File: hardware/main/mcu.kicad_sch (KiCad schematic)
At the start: 15 parts, among them Q9 SSM3J338R, U1 Holyiot-18010-NRF52840

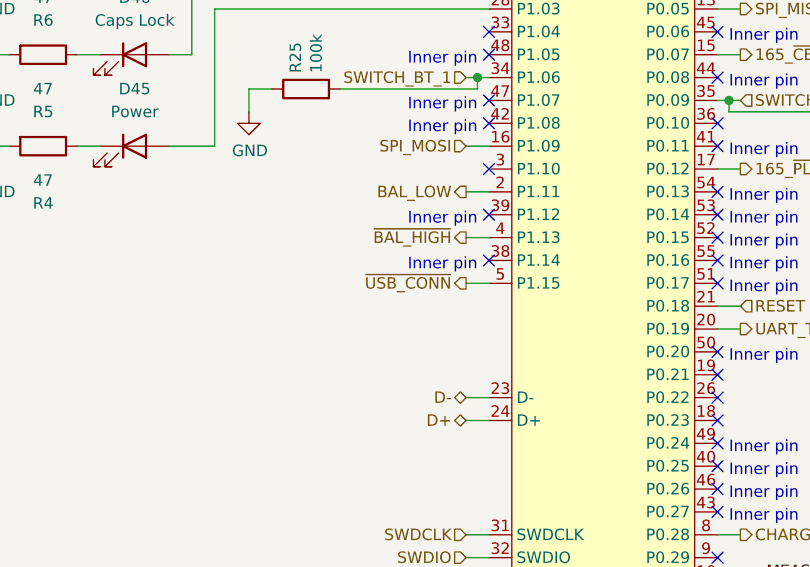
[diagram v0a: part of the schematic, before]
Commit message: Remove the USB sense curcuit
As V_BUS is connected to the MCU it can detect when the USB is
connected.
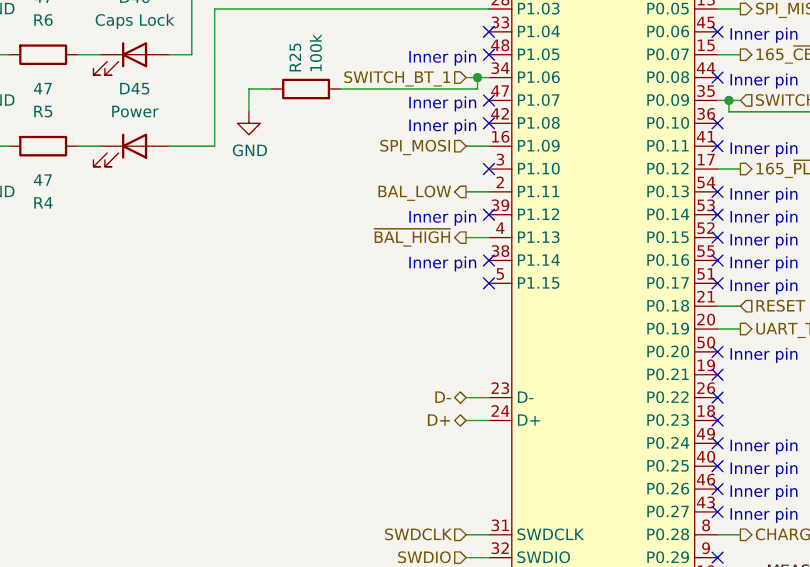
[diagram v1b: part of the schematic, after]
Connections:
- net ~USB_CONN: no longer names the net of U1.5 (P1.15)
- no-connect marks 26 -> 27
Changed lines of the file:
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@@
   (no_connect (at 127 80.01))
   (no_connect (at 127 85.09))
+  (no_connect (at 127 87.63))
   (no_connect (at 152.4 52.07))
   (no_connect (at 152.4 59.69))
@@
     (stroke (width 0) (type solid) (color 0 0 0 0))
   )
-  (wire (pts (xy 124.46 87.63) (xy 127 87.63))
-    (stroke (width 0) (type solid) (color 0 0 0 0))
-  )
   (wire (pts (xy 124.46 100.33) (xy 127 100.33))
     (stroke (width 0) (type solid) (color 0 0 0 0))
@@
     (effects (font (size 1.27 1.27)) (justify right))
   )
-  (hierarchical_label "~USB_CONN" (shape output) (at 124.46 87.63 180)
-    (effects (font (size 1.27 1.27)) (justify right))
-  )
   (hierarchical_label "D-" (shape bidirectional) (at 124.46 100.33 180)
     (effects (font (size 1.27 1.27)) (justify right))
@@
   (symbol (lib_id "power:GND") (at 179.07 71.12 0) (mirror y) (unit 1)
     (in_bom yes) (on_board yes)
-    (property "Reference" "#PWR?" (id 0) (at 179.07 77.47 0)
-      (effects (font (size 1.27 1.27)) hide)
-    )
+    (property "Reference" "#PWR0149" (id 0) (at 179.07 77.47 0)
+      (effects (font (size 1.27 1.27)) hide)
+    )

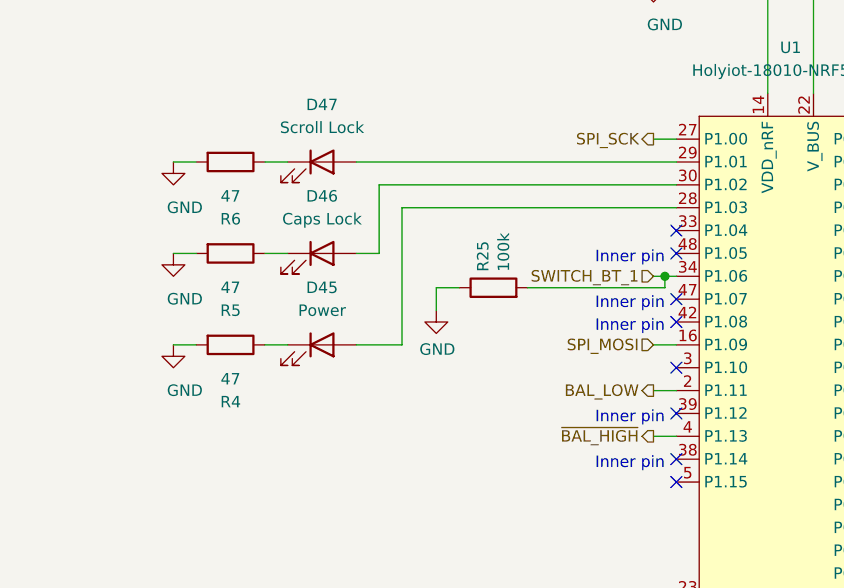
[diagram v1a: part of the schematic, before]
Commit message: Add circuit to disconnect the shift registers
This is done to save energy when the keyboard is switched off.
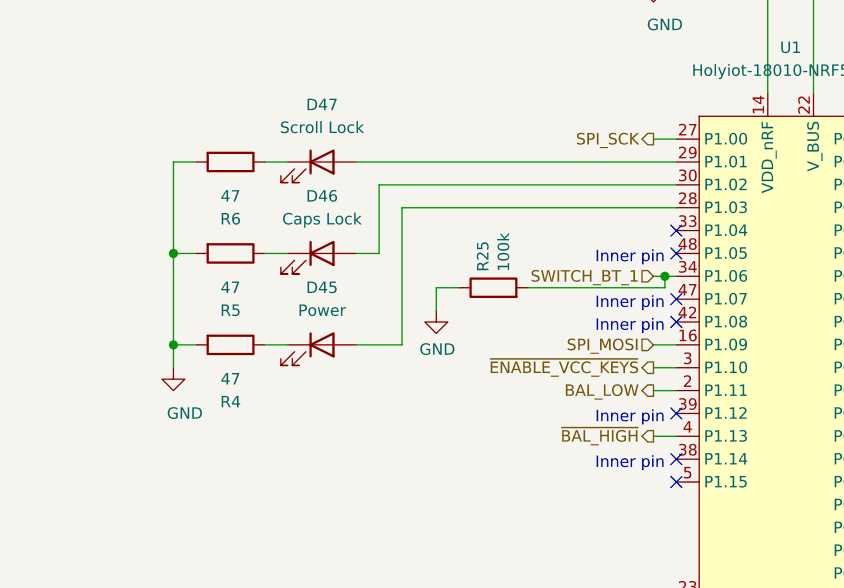
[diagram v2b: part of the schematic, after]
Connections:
- net ~ENABLE_VCC_KEYS: now reaches U1.3 (P1.10)
- no-connect marks 27 -> 26
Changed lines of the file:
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@@
   (junction (at 52.07 138.43) (diameter 1.016) (color 0 0 0 0))
   (junction (at 52.07 168.91) (diameter 1.016) (color 0 0 0 0))
+  (junction (at 71.12 62.23) (diameter 1.016) (color 0 0 0 0))
+  (junction (at 71.12 72.39) (diameter 1.016) (color 0 0 0 0))
   (junction (at 125.73 64.77) (diameter 1.016) (color 0 0 0 0))
   (junction (at 137.16 29.21) (diameter 1.016) (color 0 0 0 0))
@@
   (no_connect (at 127 67.31))
   (no_connect (at 127 69.85))
-  (no_connect (at 127 74.93))
   (no_connect (at 127 80.01))
   (no_connect (at 127 85.09))
@@
     (stroke (width 0) (type solid) (color 0 0 0 0))
   )
+  (wire (pts (xy 71.12 52.07) (xy 71.12 62.23))
+    (stroke (width 0) (type solid) (color 0 0 0 0))
+  )
   (wire (pts (xy 71.12 52.07) (xy 73.66 52.07))
     (stroke (width 0) (type solid) (color 0 0 0 0))
   )
+  (wire (pts (xy 71.12 62.23) (xy 71.12 72.39))
+    (stroke (width 0) (type solid) (color 0 0 0 0))
+  )
   (wire (pts (xy 71.12 62.23) (xy 73.66 62.23))
     (stroke (width 0) (type solid) (color 0 0 0 0))
   )
+  (wire (pts (xy 71.12 72.39) (xy 71.12 74.93))
+    (stroke (width 0) (type solid) (color 0 0 0 0))
+  )
   (wire (pts (xy 71.12 72.39) (xy 73.66 72.39))
     (stroke (width 0) (type solid) (color 0 0 0 0))
@@
   )
   (wire (pts (xy 124.46 72.39) (xy 127 72.39))
+    (stroke (width 0) (type solid) (color 0 0 0 0))
+  )
+  (wire (pts (xy 124.46 74.93) (xy 127 74.93))
     (stroke (width 0) (type solid) (color 0 0 0 0))
   )
@@
   )
   (hierarchical_label "SPI_MOSI" (shape input) (at 124.46 72.39 180)
+    (effects (font (size 1.27 1.27)) (justify right))
+  )
+  (hierarchical_label "~ENABLE_VCC_KEYS" (shape output) (at 124.46 74.93 180)
     (effects (font (size 1.27 1.27)) (justify right))
   )
@@
     )
   )
-  (symbol (lib_id "power:GND") (at 71.12 52.07 0) (unit 1)
+  (symbol (lib_id "power:GND") (at 71.12 74.93 0) (unit 1)
     (in_bom yes) (on_board yes)
-    (property "Reference" "#PWR0123" (id 0) (at 71.12 58.42 0)
-      (effects (font (size 1.27 1.27)) hide)
-    )
-    (property "Value" "GND" (id 1) (at 72.39 57.15 0))
-    (property "Footprint" "" (id 2) (at 71.12 52.07 0)
-      (effects (font (size 1.27 1.27)) hide)
-    )
-    (property "Datasheet" "" (id 3) (at 71.12 52.07 0)
-      (effects (font (size 1.27 1.27)) hide)
-    )
-  )
-  (symbol (lib_id "power:GND") (at 71.12 62.23 0) (unit 1)
-    (in_bom yes) (on_board yes)
-    (property "Reference" "#PWR0122" (id 0) (at 71.12 68.58 0)
-      (effects (font (size 1.27 1.27)) hide)
-    )
-    (property "Value" "GND" (id 1) (at 72.39 67.31 0))
-    (property "Footprint" "" (id 2) (at 71.12 62.23 0)
-      (effects (font (size 1.27 1.27)) hide)
-    )
-    (property "Datasheet" "" (id 3) (at 71.12 62.23 0)
-      (effects (font (size 1.27 1.27)) hide)
-    )
-  )
-  (symbol (lib_id "power:GND") (at 71.12 72.39 0) (unit 1)
-    (in_bom yes) (on_board yes)
-    (property "Reference" "#PWR0121" (id 0) (at 71.12 78.74 0)
-      (effects (font (size 1.27 1.27)) hide)
-    )
-    (property "Value" "GND" (id 1) (at 72.39 77.47 0))
-    (property "Footprint" "" (id 2) (at 71.12 72.39 0)
-      (effects (font (size 1.27 1.27)) hide)
-    )
-    (property "Datasheet" "" (id 3) (at 71.12 72.39 0)
-      (effects (font (size 1.27 1.27)) hide)
-    )
+    (property "Reference" "#PWR0121" (id 0) (at 71.12 81.28 0)
+      (effects (font (size 1.27 1.27)) hide)
+    )
+    (property "Value" "GND" (id 1) (at 72.39 80.01 0))
+    (property "Footprint" "" (id 2) (at 71.12 74.93 0)
+      (effects (font (size 1.27 1.27)) hide)
+    )
+    (property "Datasheet" "" (id 3) (at 71.12 74.93 0)
+      (effects (font (size 1.27 1.27)) hide)
+    )

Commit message: Rework the connection to the numpad
Changes:
- The UART lines now have a protection circuit
- The power supply line of the numpad can be switched on and off by the MCU.
- An Id-line is added so that the MCU can detect when the numpad is
  connected.
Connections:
- net ~NUMPAD_ID: now reaches U1.33 (P1.04)
- net ~ENABLE_VCC_NUMPAD: now reaches U1.36 (P0.10)
- no-connect marks 26 -> 24
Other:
- moved on the sheet: R26
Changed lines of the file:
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@@
   (junction (at 142.24 29.21) (diameter 1.016) (color 0 0 0 0))
   (junction (at 153.67 67.31) (diameter 1.016) (color 0 0 0 0))
-  (no_connect (at 127 59.69))
   (no_connect (at 127 62.23))
   (no_connect (at 127 67.31))
@@
   (no_connect (at 152.4 59.69))
   (no_connect (at 152.4 64.77))
-  (no_connect (at 152.4 69.85))
   (no_connect (at 152.4 72.39))
   (no_connect (at 152.4 77.47))
@@
     (stroke (width 0) (type solid) (color 0 0 0 0))
   )
+  (wire (pts (xy 124.46 59.69) (xy 127 59.69))
+    (stroke (width 0) (type solid) (color 0 0 0 0))
+  )
   (wire (pts (xy 124.46 64.77) (xy 125.73 64.77))
     (stroke (width 0) (type solid) (color 0 0 0 0))
@@
     (stroke (width 0) (type solid) (color 0 0 0 0))
   )
+  (wire (pts (xy 152.4 69.85) (xy 153.67 69.85))
+    (stroke (width 0) (type solid) (color 0 0 0 0))
+  )
   (wire (pts (xy 152.4 74.93) (xy 154.94 74.93))
     (stroke (width 0) (type solid) (color 0 0 0 0))
@@
     (stroke (width 0) (type solid) (color 0 0 0 0))
   )
+  (wire (pts (xy 153.67 66.04) (xy 153.67 67.31))
+    (stroke (width 0) (type solid) (color 0 0 0 0))
+  )
   (wire (pts (xy 153.67 67.31) (xy 154.94 67.31))
     (stroke (width 0) (type solid) (color 0 0 0 0))
   )
-  (wire (pts (xy 153.67 68.58) (xy 153.67 67.31))
-    (stroke (width 0) (type solid) (color 0 0 0 0))
-  )
   (wire (pts (xy 154.94 29.21) (xy 154.94 31.75))
     (stroke (width 0) (type solid) (color 0 0 0 0))
@@
     (stroke (width 0) (type solid) (color 0 0 0 0))
   )
-  (wire (pts (xy 168.91 68.58) (xy 153.67 68.58))
-    (stroke (width 0) (type solid) (color 0 0 0 0))
-  )
-  (wire (pts (xy 179.07 68.58) (xy 176.53 68.58))
-    (stroke (width 0) (type solid) (color 0 0 0 0))
-  )
-  (wire (pts (xy 179.07 68.58) (xy 179.07 71.12))
+  (wire (pts (xy 179.07 66.04) (xy 153.67 66.04))
+    (stroke (width 0) (type solid) (color 0 0 0 0))
+  )
+  (wire (pts (xy 189.23 66.04) (xy 186.69 66.04))
+    (stroke (width 0) (type solid) (color 0 0 0 0))
+  )
+  (wire (pts (xy 189.23 66.04) (xy 189.23 68.58))
     (stroke (width 0) (type solid) (color 0 0 0 0))
   )
@@
     (effects (font (size 1.27 1.27)) (justify right))
   )
+  (hierarchical_label "~NUMPAD_ID" (shape input) (at 124.46 59.69 180)
+    (effects (font (size 1.27 1.27)) (justify right))
+  )
   (hierarchical_label "SWITCH_BT_1" (shape input) (at 124.46 64.77 180)
     (effects (font (size 1.27 1.27)) (justify right))
@@
   )
   (hierarchical_label "VCC_SW" (shape input) (at 137.16 25.4 90)
+    (effects (font (size 1.27 1.27)) (justify left))
+  )
+  (hierarchical_label "~ENABLE_VCC_NUMPAD" (shape output) (at 153.67 69.85 0)
     (effects (font (size 1.27 1.27)) (justify left))
   )
@@
     )
   )
-  (symbol (lib_id "power:GND") (at 179.07 71.12 0) (mirror y) (unit 1)
-    (in_bom yes) (on_board yes)
-    (property "Reference" "#PWR0149" (id 0) (at 179.07 77.47 0)
-      (effects (font (size 1.27 1.27)) hide)
-    )
-    (property "Value" "GND" (id 1) (at 178.9557 75.4444 0))
-    (property "Footprint" "" (id 2) (at 179.07 71.12 0)
-      (effects (font (size 1.27 1.27)) hide)
-    )
-    (property "Datasheet" "" (id 3) (at 179.07 71.12 0)
+  (symbol (lib_id "power:GND") (at 189.23 68.58 0) (mirror y) (unit 1)
+    (in_bom yes) (on_board yes)
+    (property "Reference" "#PWR0149" (id 0) (at 189.23 74.93 0)
+      (effects (font (size 1.27 1.27)) hide)
+    )
+    (property "Value" "GND" (id 1) (at 189.1157 72.9044 0))
+    (property "Footprint" "" (id 2) (at 189.23 68.58 0)
+      (effects (font (size 1.27 1.27)) hide)
+    )
+    (property "Datasheet" "" (id 3) (at 189.23 68.58 0)
       (effects (font (size 1.27 1.27)) hide)
     )
@@
     )
   )
-  (symbol (lib_id "Device:R") (at 172.72 68.58 90) (unit 1)
-    (in_bom yes) (on_board yes)
-    (property "Reference" "R26" (id 0) (at 171.5706 66.8019 0)
-      (effects (font (size 1.27 1.27)) (justify left))
-    )
-    (property "Value" "100k" (id 1) (at 173.8693 66.8019 0)
-      (effects (font (size 1.27 1.27)) (justify left))
-    )
-    (property "Footprint" "Resistor_SMD:R_0603_1608Metric_Pad0.98x0.95mm_HandSolder" (id 2) (at 172.72 70.358 90)
-      (effects (font (size 1.27 1.27)) hide)
-    )
-    (property "Datasheet" "~" (id 3) (at 172.72 68.58 0)
-      (effects (font (size 1.27 1.27)) hide)
-    )
+  (symbol (lib_id "Device:R") (at 182.88 66.04 90) (unit 1)
+    (in_bom yes) (on_board yes)
+    (property "Reference" "R26" (id 0) (at 181.7306 64.2619 0)
+      (effects (font (size 1.27 1.27)) (justify left))
+    )
+    (property "Value" "100k" (id 1) (at 184.0293 64.2619 0)
+      (effects (font (size 1.27 1.27)) (justify left))
+    )
+    (property "Footprint" "Resistor_SMD:R_0603_1608Metric_Pad0.98x0.95mm_HandSolder" (id 2) (at 182.88 67.818 90)
+      (effects (font (size 1.27 1.27)) hide)
+    )
+    (property "Datasheet" "~" (id 3) (at 182.88 66.04 0)
+      (effects (font (size 1.27 1.27)) hide)
+    )

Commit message: WIP: Design of PCB
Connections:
- net MEAS_V_BATT: now also U1.11 (P0.31); no longer U1.10 (P0.30)
- net SPI_MOSI: now also U1.12 (P0.04); no longer U1.16 (P1.09)
- net UART_RX: now also U1.19 (P0.21); no longer U1.12 (P0.04)
- net ~ACT_MEAS_V_BATT: now also U1.10 (P0.30); no longer U1.11 (P0.31)
- net ~ENABLE_VCC_KEYS: now also U1.26 (P0.22); no longer U1.3 (P1.10)
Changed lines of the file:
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@@
   (no_connect (at 127 67.31))
   (no_connect (at 127 69.85))
+  (no_connect (at 127 72.39))
+  (no_connect (at 127 74.93))
   (no_connect (at 127 80.01))
   (no_connect (at 127 85.09))
@@
   (no_connect (at 152.4 87.63))
   (no_connect (at 152.4 95.25))
-  (no_connect (at 152.4 97.79))
-  (no_connect (at 152.4 100.33))
   (no_connect (at 152.4 102.87))
   (no_connect (at 152.4 105.41))
@@
     (stroke (width 0) (type solid) (color 0 0 0 0))
   )
-  (wire (pts (xy 124.46 72.39) (xy 127 72.39))
-    (stroke (width 0) (type solid) (color 0 0 0 0))
-  )
-  (wire (pts (xy 124.46 74.93) (xy 127 74.93))
-    (stroke (width 0) (type solid) (color 0 0 0 0))
-  )
   (wire (pts (xy 124.46 77.47) (xy 127 77.47))
     (stroke (width 0) (type solid) (color 0 0 0 0))
@@
     (stroke (width 0) (type solid) (color 0 0 0 0))
   )
+  (wire (pts (xy 152.4 100.33) (xy 154.94 100.33))
+    (stroke (width 0) (type solid) (color 0 0 0 0))
+  )
   (wire (pts (xy 152.4 115.57) (xy 154.94 115.57))
     (stroke (width 0) (type solid) (color 0 0 0 0))
@@
   )
   (wire (pts (xy 154.94 57.15) (xy 152.4 57.15))
+    (stroke (width 0) (type solid) (color 0 0 0 0))
+  )
+  (wire (pts (xy 154.94 97.79) (xy 152.4 97.79))
     (stroke (width 0) (type solid) (color 0 0 0 0))
   )
@@
     (effects (font (size 1.27 1.27)) (justify right bottom))
   )
-  (label "MEAS_V_BATT" (at 170.18 120.65 180)
-    (effects (font (size 1.27 1.27)) (justify right bottom))
-  )
-  (label "~ACT_MEAS_V_BATT" (at 170.18 123.19 180)
+  (label "~ACT_MEAS_V_BATT" (at 170.18 120.65 180)
+    (effects (font (size 1.27 1.27)) (justify right bottom))
+  )
+  (label "MEAS_V_BATT" (at 170.18 123.19 180)
     (effects (font (size 1.27 1.27)) (justify right bottom))
   )
@@
     (effects (font (size 1.27 1.27)) (justify right))
   )
-  (hierarchical_label "SPI_MOSI" (shape input) (at 124.46 72.39 180)
-    (effects (font (size 1.27 1.27)) (justify right))
-  )
-  (hierarchical_label "~ENABLE_VCC_KEYS" (shape output) (at 124.46 74.93 180)
-    (effects (font (size 1.27 1.27)) (justify right))
-  )
   (hierarchical_label "BAL_LOW" (shape output) (at 124.46 77.47 180)
     (effects (font (size 1.27 1.27)) (justify right))
@@
     (effects (font (size 1.27 1.27)) (justify left))
   )
-  (hierarchical_label "UART_RX" (shape input) (at 154.94 54.61 0)
+  (hierarchical_label "SPI_MOSI" (shape input) (at 154.94 54.61 0)
     (effects (font (size 1.27 1.27)) (justify left))
   )
@@
     (effects (font (size 1.27 1.27)) (justify left))
   )
+  (hierarchical_label "UART_RX" (shape input) (at 154.94 97.79 0)
+    (effects (font (size 1.27 1.27)) (justify left))
+  )
+  (hierarchical_label "~ENABLE_VCC_KEYS" (shape output) (at 154.94 100.33 0)
+    (effects (font (size 1.27 1.27)) (justify left))
+  )

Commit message: WIP: Design of PCB
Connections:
- net 165_~CE: now also U1.17 (P0.12); no longer U1.15 (P0.07)
- net 165_~PL: now also U1.15 (P0.07); no longer U1.17 (P0.12)
- net SPI_MISO: now also U1.12 (P0.04); no longer U1.13 (P0.05)
- net SPI_MOSI: now also U1.13 (P0.05); no longer U1.12 (P0.04)
- net at D47.2 (A): now also U1.30 (P1.02); no longer U1.29 (P1.01)
- net at D46.2 (A): now also U1.29 (P1.01); no longer U1.30 (P1.02)
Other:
- moved on the sheet: D46, D47, R5, R6
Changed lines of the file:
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@@
     (effects (font (size 1.27 1.27)) (justify left))
   )
-  (hierarchical_label "SPI_MOSI" (shape input) (at 154.94 54.61 0)
-    (effects (font (size 1.27 1.27)) (justify left))
-  )
-  (hierarchical_label "SPI_MISO" (shape output) (at 154.94 57.15 0)
-    (effects (font (size 1.27 1.27)) (justify left))
-  )
-  (hierarchical_label "165_~CE" (shape output) (at 154.94 62.23 0)
+  (hierarchical_label "SPI_MISO" (shape output) (at 154.94 54.61 0)
+    (effects (font (size 1.27 1.27)) (justify left))
+  )
+  (hierarchical_label "SPI_MOSI" (shape input) (at 154.94 57.15 0)
+    (effects (font (size 1.27 1.27)) (justify left))
+  )
+  (hierarchical_label "165_~PL" (shape output) (at 154.94 62.23 0)
     (effects (font (size 1.27 1.27)) (justify left))
   )
@@
     (effects (font (size 1.27 1.27)) (justify left))
   )
-  (hierarchical_label "165_~PL" (shape output) (at 154.94 74.93 0)
+  (hierarchical_label "165_~CE" (shape output) (at 154.94 74.93 0)
     (effects (font (size 1.27 1.27)) (justify left))
   )
@@
   (symbol (lib_id "Device:R") (at 77.47 52.07 270) (unit 1)
     (in_bom yes) (on_board yes)
-    (property "Reference" "R6" (id 0) (at 77.47 58.42 90))
+    (property "Reference" "R5" (id 0) (at 77.47 58.42 90))
     (property "Value" "47" (id 1) (at 77.47 55.88 90))
     (property "Footprint" "Resistor_SMD:R_0603_1608Metric_Pad0.98x0.95mm_HandSolder" (id 2) (at 77.47 50.292 90)
@@
   (symbol (lib_id "Device:R") (at 77.47 62.23 270) (unit 1)
     (in_bom yes) (on_board yes)
-    (property "Reference" "R5" (id 0) (at 77.47 68.58 90))
+    (property "Reference" "R6" (id 0) (at 77.47 68.58 90))
     (property "Value" "47" (id 1) (at 77.47 66.04 90))
     (property "Footprint" "Resistor_SMD:R_0603_1608Metric_Pad0.98x0.95mm_HandSolder" (id 2) (at 77.47 60.452 90)
@@
   (symbol (lib_id "Device:LED") (at 87.63 52.07 0) (unit 1)
     (in_bom yes) (on_board yes)
-    (property "Reference" "D47" (id 0) (at 87.63 45.72 0))
-    (property "Value" "Scroll Lock" (id 1) (at 87.63 48.26 0))
+    (property "Reference" "D46" (id 0) (at 87.63 45.72 0))
+    (property "Value" "Caps Lock" (id 1) (at 87.63 48.26 0))
     (property "Footprint" "Diode_SMD:D_0603_1608Metric_Pad1.05x0.95mm_HandSolder" (id 2) (at 87.63 52.07 0)
       (effects (font (size 1.27 1.27)) hide)
@@
   (symbol (lib_id "Device:LED") (at 87.63 62.23 0) (unit 1)
     (in_bom yes) (on_board yes)
-    (property "Reference" "D46" (id 0) (at 87.63 55.88 0))
-    (property "Value" "Caps Lock" (id 1) (at 87.63 58.42 0))
+    (property "Reference" "D47" (id 0) (at 87.63 55.88 0))
+    (property "Value" "Scroll Lock" (id 1) (at 87.63 58.42 0))
     (property "Footprint" "Diode_SMD:D_0603_1608Metric_Pad1.05x0.95mm_HandSolder" (id 2) (at 87.63 62.23 0)
       (effects (font (size 1.27 1.27)) hide)

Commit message: Re-add USB voltage sense circuit
Due to firmware limitations the USB voltage cannot be used directly for
waking up the microcontroller.
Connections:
- net ~USB_CONN: now reaches U1.18 (P0.23)
- no-connect marks 24 -> 23
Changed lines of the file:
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@@
   (no_connect (at 152.4 87.63))
   (no_connect (at 152.4 95.25))
-  (no_connect (at 152.4 102.87))
   (no_connect (at 152.4 105.41))
   (no_connect (at 152.4 107.95))
@@
     (stroke (width 0) (type solid) (color 0 0 0 0))
   )
+  (wire (pts (xy 152.4 102.87) (xy 154.94 102.87))
+    (stroke (width 0) (type solid) (color 0 0 0 0))
+  )
   (wire (pts (xy 152.4 115.57) (xy 154.94 115.57))
     (stroke (width 0) (type solid) (color 0 0 0 0))
@@
     (effects (font (size 1.27 1.27)) (justify left))
   )
+  (hierarchical_label "~USB_CONN" (shape input) (at 154.94 102.87 0)
+    (effects (font (size 1.27 1.27)) (justify left))
+  )
